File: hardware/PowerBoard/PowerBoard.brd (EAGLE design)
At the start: 90 x 56 mm, 134 parts, among them J1 CON-HRS-DM3AT, J2 CON-ZX62R-B-5P, J3 CON-FTSH-105-01-L-DV-K, J4 CON-S2B-PH-SM4-TB, J5 CON-PJ-102A, J6 CON-71741-0002-TOP, M1 MOUNT-HOLE3.3, M2 MOUNT-HOLE3.3, M3 MOUNT-HOLE3.3, M4 MOUNT-HOLE3.3, M5 FIDUCIAL1X2, M6 FIDUCIAL1X2, M7 FIDUCIAL1X2, M8 FIDUCIAL1X2, Q1 SI2323CDS, Q2 SI2312CDS, Q3 SI2333CDS, Q4 SI2333CDS, SW1 SWITCH-SPST, SW2 SWITCH-MS12ASG30, SW3 SWITCH-KSC-201J, U1 LTC4361-2DC, U10 MAX9938FEUK, U11 MAX9938FEUK, U12 MAX9938FEUK, U13 STM32F10XCXT6, U14 LTC2942-1, U15 USBLC6-2, U2 LTC4085, U3 XC6220B331MR-G, U4 XC6220B331MR-G, U5 XC9236A15DMR-G, U6 MIC94043, U8 MAX9938FEUK, U9 MAX9938FEUK, X1 ECX-2236, X2 ECX-31B

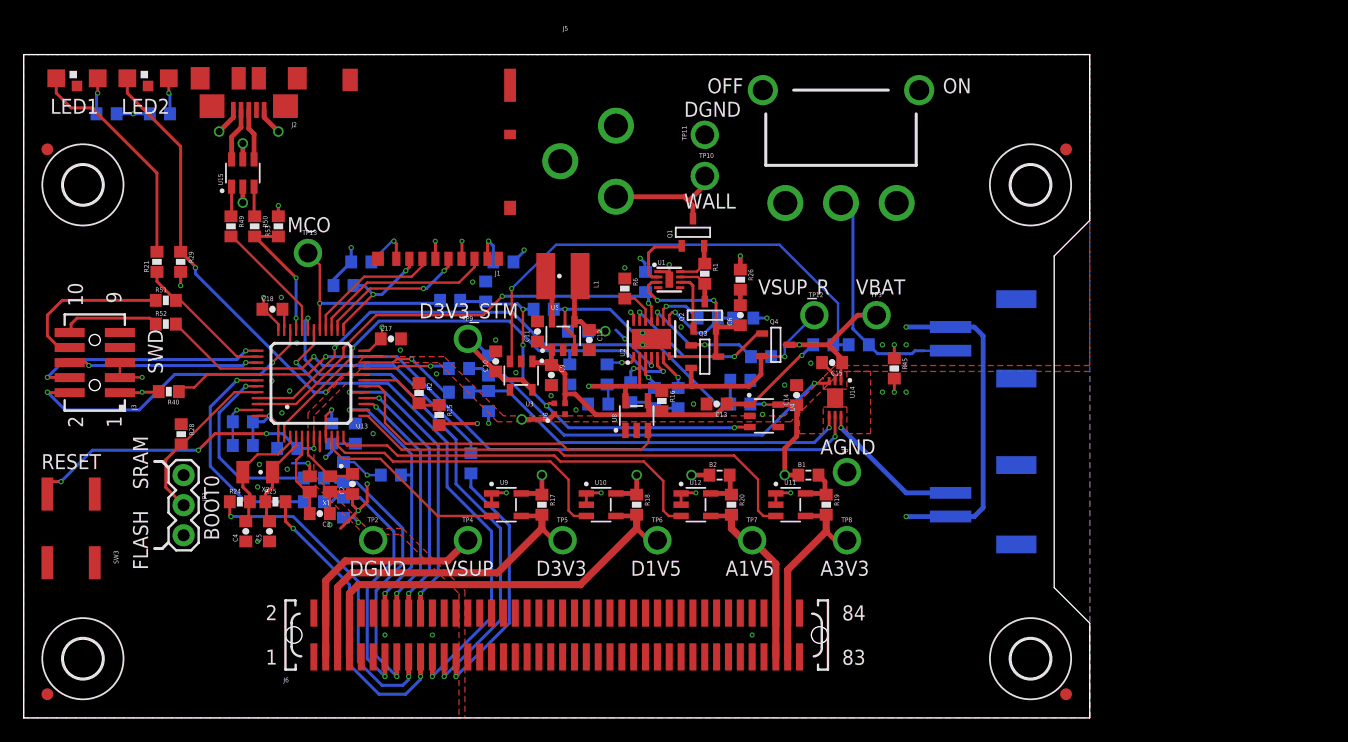
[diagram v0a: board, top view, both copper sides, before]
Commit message: - Interface updated on schematic
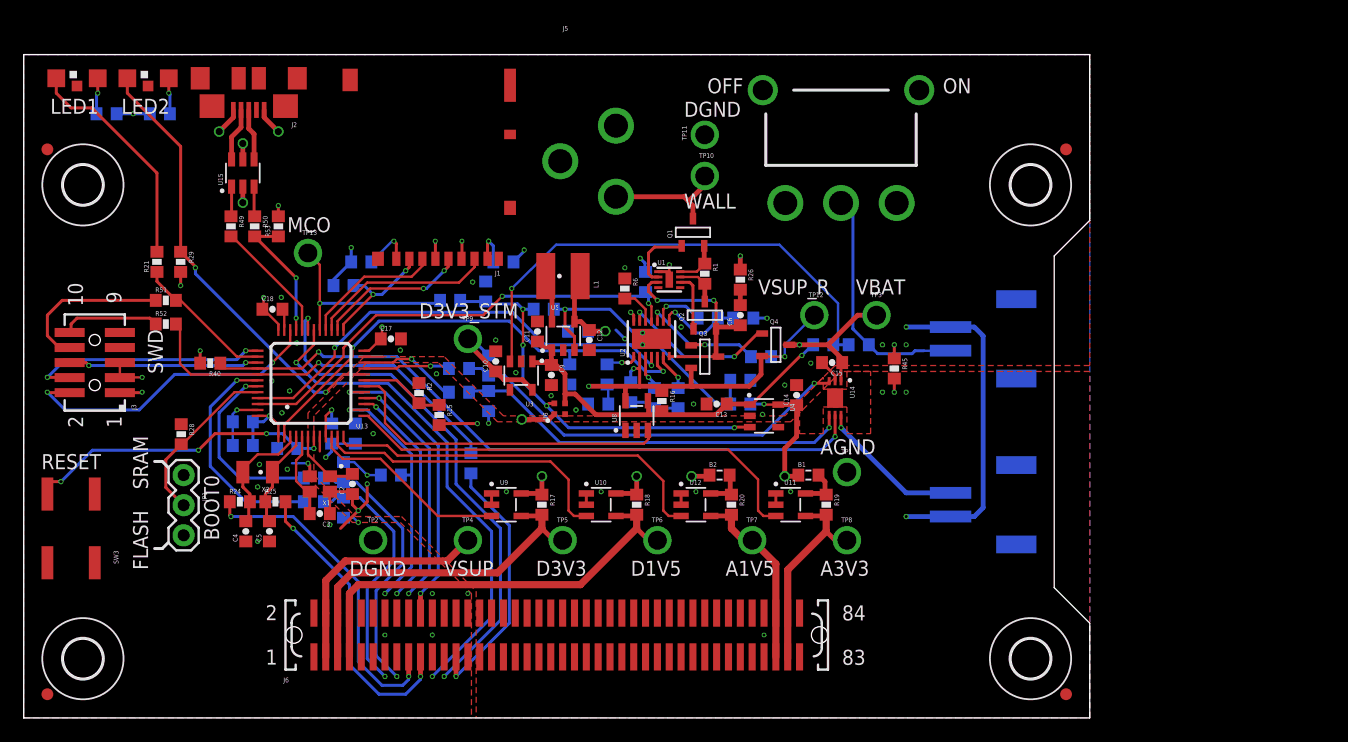
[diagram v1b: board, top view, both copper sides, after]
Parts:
- moved R40 4.24 mm to (15.8, 29.9)
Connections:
- net AGND: now also J6.77, J6.78; no longer J6.75, J6.76
- net DGND: now also J6.10, J6.15, J6.16, J6.9; no longer J6.11, J6.12, J6.22
- net I2C1_SCL: now also J6.26; no longer J6.13
- net I2C1_SDA: now also J6.28; no longer J6.15
- net PA10: now also J6.21; no longer J6.23
- net PA9: now also J6.23; no longer J6.21
- net PB4: now also R40.1, U14.5; no longer R48.2, R52.2
- net PB5: now also R48.2, R52.2; no longer R40.1, U14.5
- net SPI1_MISO: now also J6.22; no longer J6.18
- net SPI1_NSS: now also J6.24; no longer J6.14
- net SPI1_SCK: now also J6.18; no longer J6.16
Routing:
- net PB5: track 61.3 -> 32.0 mm, vias 2 -> 1
- net PB4: track 30.8 -> 58.3 mm, vias 1 -> 2
- net AGND: track 14.8 -> 9.76 mm
- net SPI1_SCK: track 20.9 -> 19.2 mm
- net SPI1_NSS: track 23.2 -> 21.6 mm
- net SPI1_MISO: track 21.9 -> 20.2 mm
- net PA9: track 43.9 -> 42.3 mm
- net PA10: track 45.3 -> 43.7 mm
- net I2C1_SDA: track 24.2 -> 22.6 mm
- net I2C1_SCL: track 22.7 -> 21.0 mm
- net VSUP_I_SENSE: track 29.0 -> 28.4 mm
- net D3V3_STM: track 50.8 -> 50.5 mm, vias 15 -> 16
- net DGND: vias 43 -> 45

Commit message: - Layout update - Interface update
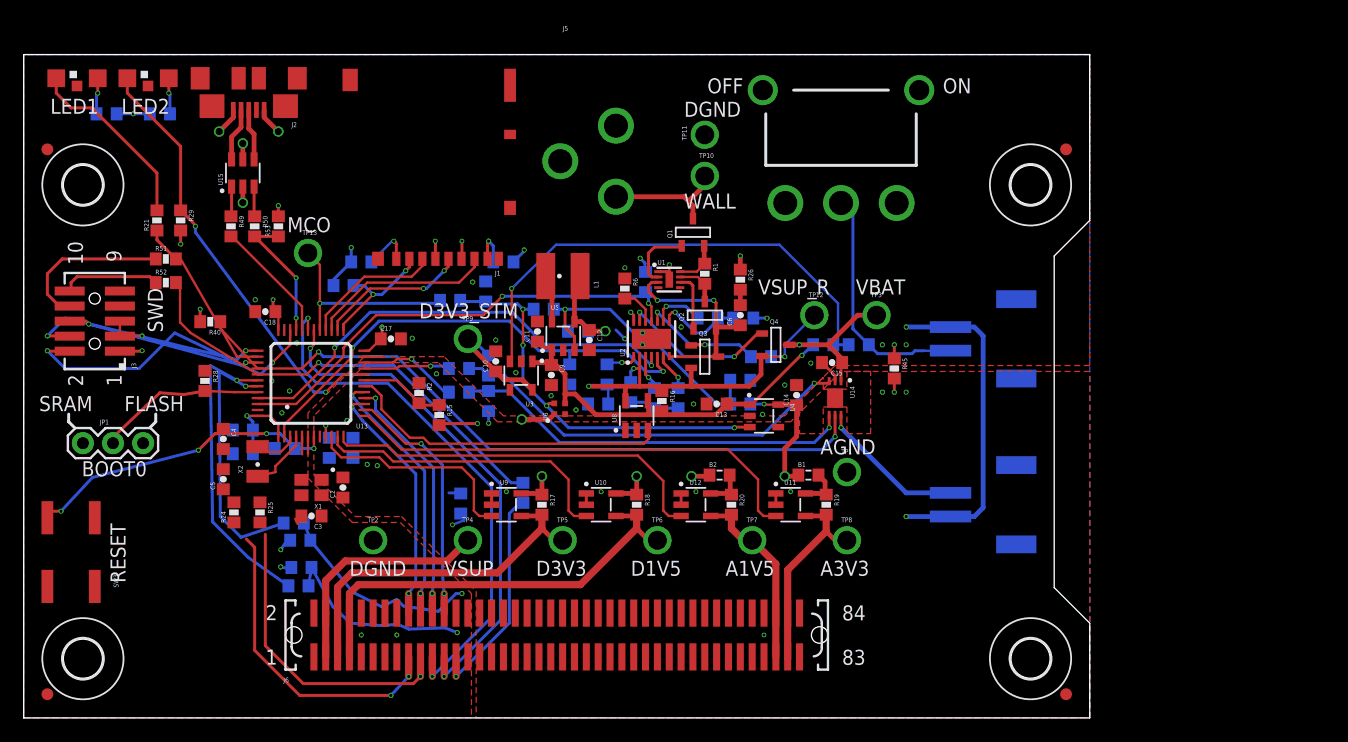
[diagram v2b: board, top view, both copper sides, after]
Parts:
- moved JP1 8.92 mm to (5.00, 23.2), turned to 0 degrees
- moved C4 8.03 mm to (16.9, 23.6), turned to 270 degrees
- moved R34 7.22 mm to (23.2, 11.2)
- moved R33 6.81 mm to (23.4, 15.0), turned to 0 degrees
- moved R30 6.37 mm to (36.9, 18.1), turned to 270 degrees
- moved R32 6.17 mm to (23.4, 12.7), turned to 0 degrees
- moved C5 5.88 mm to (16.9, 20.1)
- moved R48 5.06 mm to (42.1, 19.0)
- moved R28 4.92 mm to (15.3, 28.4)
- moved R35 4.16 mm to (22.8, 16.4)
- moved R40 3.50 mm to (15.8, 33.5)
- moved J3 3.50 mm to (6.00, 33.5)
- moved R21 3.50 mm to (11.2, 42.0)
- moved R29 3.50 mm to (13.2, 42.0)
- moved R51 3.50 mm to (12.0, 38.8)
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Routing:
- net DGND: track 71.1 -> 51.8 mm, vias 45 -> 35
- net D3V3_STM: track 50.5 -> 43.7 mm, vias 16 -> 17
- net I2C1_SCLI: track 19.1 -> 25.9 mm
- net PC14-S: track 10.2 -> 3.38 mm
- net I2C1_SDAI: track 15.8 -> 22.1 mm
- net PB5: track 32.0 -> 37.9 mm
- net OSC_IN: track 7.33 -> 1.50 mm
- net I2C1_SDA: track 22.6 -> 17.7 mm
- net AGND: track 9.76 -> 5.15 mm
- net OSC_OUT: track 6.10 -> 1.50 mm
- net I2C1_SCL: track 21.0 -> 17.3 mm
- net PB4-SF: track 22.0 -> 18.5 mm
- net PA15-LED1: track 19.5 -> 16.0 mm
- net SPI1_MOSI: track 25.4 -> 22.1 mm
- net PC15-S: track 8.52 -> 5.27 mm
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
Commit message: - Layout update
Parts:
- moved TP2 17.0 mm to (12.5, 15.0)
- moved TP4 17.0 mm to (20.5, 15.0)
- moved TP5 17.0 mm to (28.5, 15.0)
- moved TP6 17.0 mm to (36.5, 15.0)
- moved R17 10.0 mm to (33.8, 18.0)
- moved R18 10.0 mm to (41.8, 18.0)
- moved U10 10.0 mm to (38.8, 18.0)
- moved U9 10.0 mm to (30.8, 18.0)
- moved TP7 8.00 mm to (53.5, 15.0)
- moved TP8 8.00 mm to (61.5, 15.0)
- moved B2 7.50 mm to (51.2, 20.5)
- moved R19 7.50 mm to (60.2, 18.0)
- moved U11 7.50 mm to (57.2, 18.0)
- moved R20 7.30 mm to (52.5, 18.0)
- moved U12 7.30 mm to (49.5, 18.0)
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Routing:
- net D1V5: track 37.0 -> 24.4 mm
- net D3V3: track 30.3 -> 18.7 mm
- net D3V3_I: track 36.9 -> 47.8 mm
- net D1V5_SENSE: track 25.7 -> 15.7 mm
- net D3V3_SENSE: track 18.4 -> 8.76 mm
- net I2C1_SCLI: track 25.9 -> 16.4 mm
- net I2C1_SDA: track 17.7 -> 26.1 mm
- net PB4-SF: track 18.5 -> 10.6 mm
- net A3V3_SENSE: track 39.5 -> 32.0 mm
- net A1V5_SENSE: track 32.6 -> 25.3 mm
- net PB5: track 37.9 -> 44.9 mm
- net I2C1_SDAI: track 22.1 -> 15.2 mm
- net A1V5: track 15.8 -> 21.8 mm
- net VSUP: track 34.9 -> 39.7 mm
- net NRST: track 26.2 -> 30.2 mm, vias 4 -> 2
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
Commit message: - Layout
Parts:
- moved C4 3.61 mm to (16.8, 19.1)
- moved R28 2.55 mm to (13.2, 24.1)
- moved R32 1.71 mm to (26.1, 12.6), turned to 180 degrees
- moved R33 1.64 mm to (23.1, 12.6), turned to 0 degrees
- moved R40 1.53 mm to (17.2, 30.8), turned to 90 degrees
- moved C2 1.48 mm to (26.8, 18.4)
- moved R24 1.29 mm to (15.6, 15.1)
- moved R25 1.25 mm to (17.6, 15.1)
- moved C16 1.12 mm to (21.1, 22.2)
- moved R34 0.95 mm to (25.6, 15.1)
- moved R35 0.95 mm to (23.6, 15.1)
- moved C5 0.92 mm to (20.9, 18.4), turned to 90 degrees
- moved X1 0.92 mm to (24.2, 20.1)
- moved C3 0.76 mm to (24.2, 17.6)
- moved X2 0.36 mm to (19.8, 21.1), turned to 180 degrees
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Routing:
- net I2C1_SDA: track 26.1 -> 18.8 mm
- net OSC_IN: track 1.50 -> 6.10 mm
- net OSC_OUT: track 1.50 -> 5.37 mm
- net I2C1_SCL: track 19.2 -> 16.0 mm
- net D3V3_STM: track 42.5 -> 44.8 mm, vias 16 -> 17
- net TRACESWO: track 16.5 -> 18.4 mm
- net PC14-S: track 3.36 -> 4.61 mm
- net PC15-S: track 4.36 -> 3.16 mm
- net I2C1_SDAI: track 15.2 -> 14.1 mm
- net PC15: track 26.4 -> 25.4 mm
- net PC14: track 28.6 -> 27.6 mm
- net SWCLK: track 20.6 -> 21.5 mm
- net NRST: track 30.2 -> 30.9 mm
- net PB5: track 44.9 -> 44.3 mm
- net SWDIO: track 25.3 -> 25.8 mm

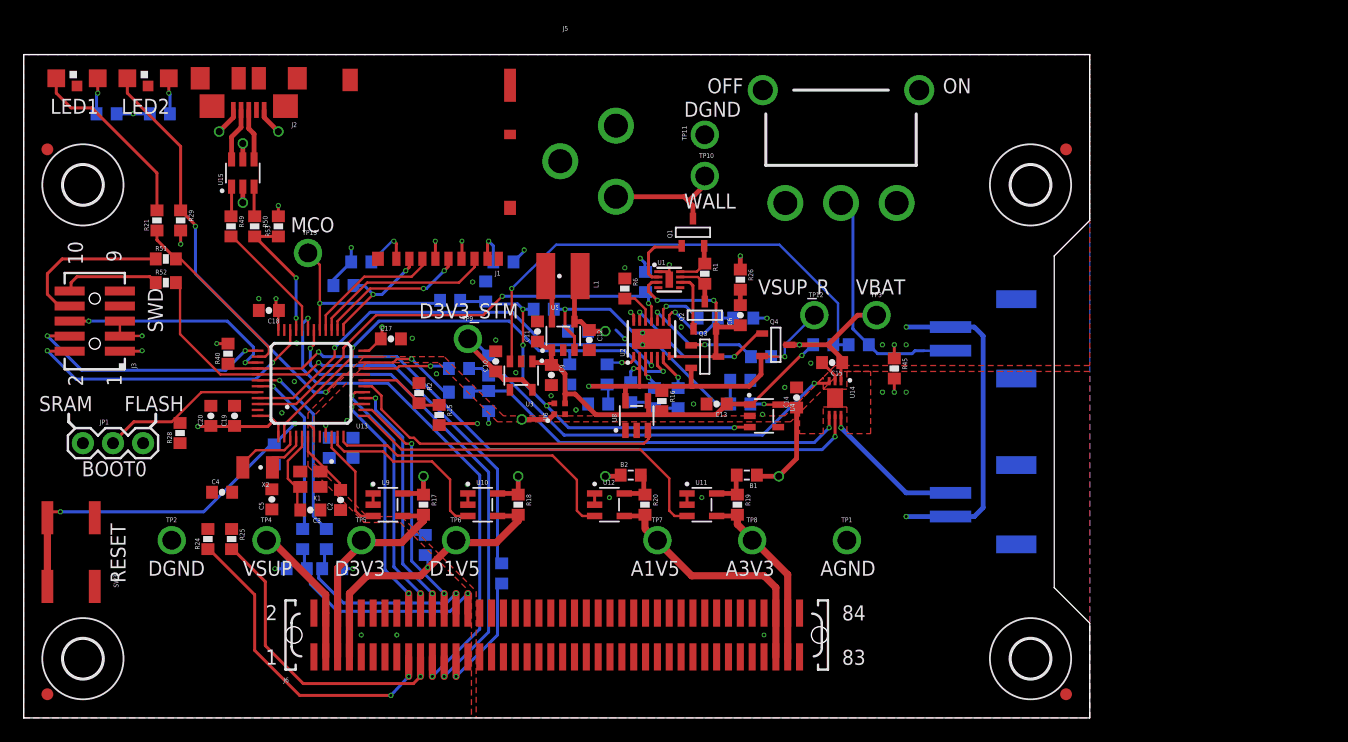
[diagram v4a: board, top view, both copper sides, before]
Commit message: - Components moved out of the bottom keep-out-box representing the battery - All grounds connected to mezzanine interface
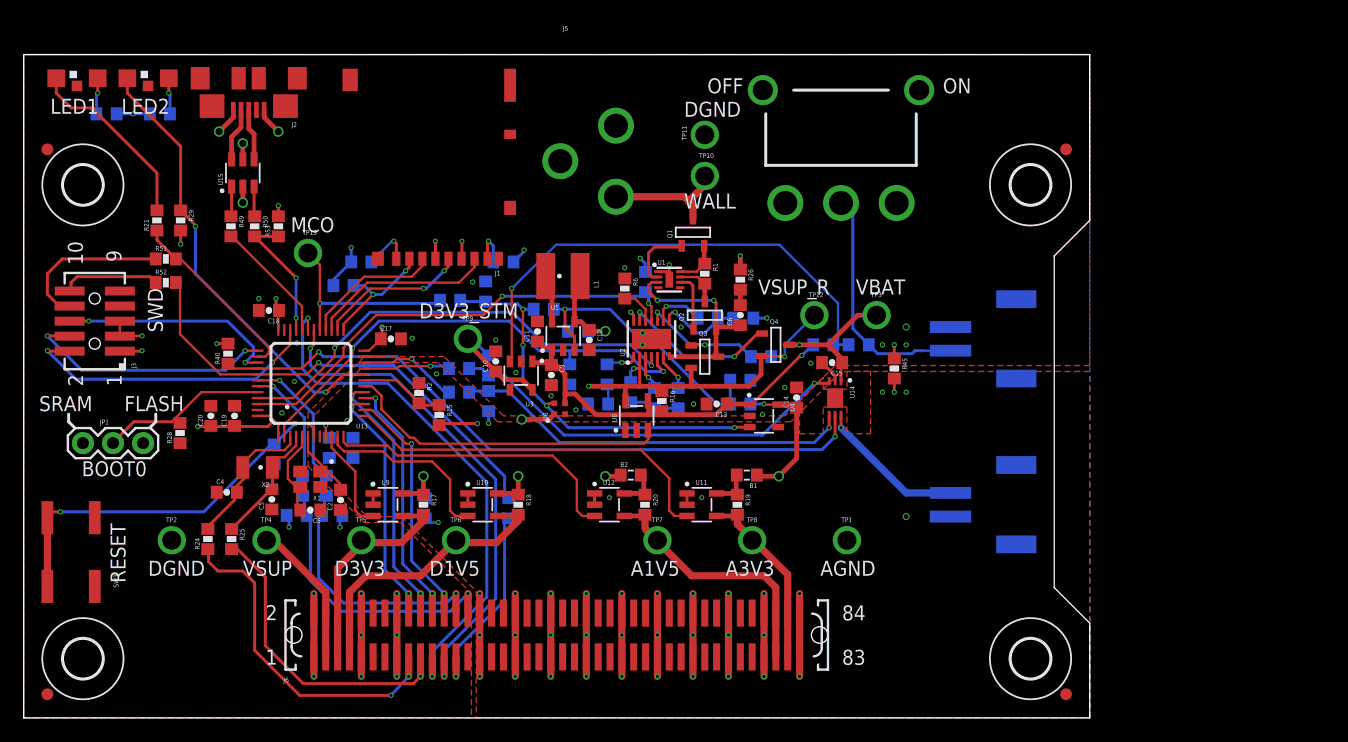
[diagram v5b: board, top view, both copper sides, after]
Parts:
- moved R48 5.53 mm to (41.0, 17.7)
- moved R32 4.50 mm to (26.1, 17.1)
- moved R33 4.50 mm to (23.1, 17.1)
- moved R34 4.50 mm to (25.6, 19.6)
- moved R35 4.50 mm to (23.6, 19.6)
- moved R30 3.10 mm to (33.9, 17.7)
- moved C4 0.40 mm to (17.1, 19.1)
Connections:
- net AGND: now also J6.29, J6.30, J6.35, J6.36, J6.41, J6.42, J6.47, J6.48, J6.53, J6.54, J6.59, J6.60, J6.65, J6.66, J6.71, J6.72
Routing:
- net AGND: track 5.15 -> 75.2 mm, vias 10 -> 38
- net DGND: track 51.2 -> 43.3 mm, vias 33 -> 38
- net PB4-SF: track 10.6 -> 16.9 mm
- net PC15-S: track 3.16 -> 9.23 mm
- net PB5: track 44.3 -> 38.6 mm
- net PC14-S: track 4.61 -> 9.92 mm
- net I2C1_SCL: track 16.0 -> 21.0 mm
- net I2C1_SDA: track 18.8 -> 23.3 mm
- net I2C1_SDAI: track 14.1 -> 9.60 mm
- net I2C1_SCLI: track 16.0 -> 11.5 mm

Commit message: - Minor changes in layout
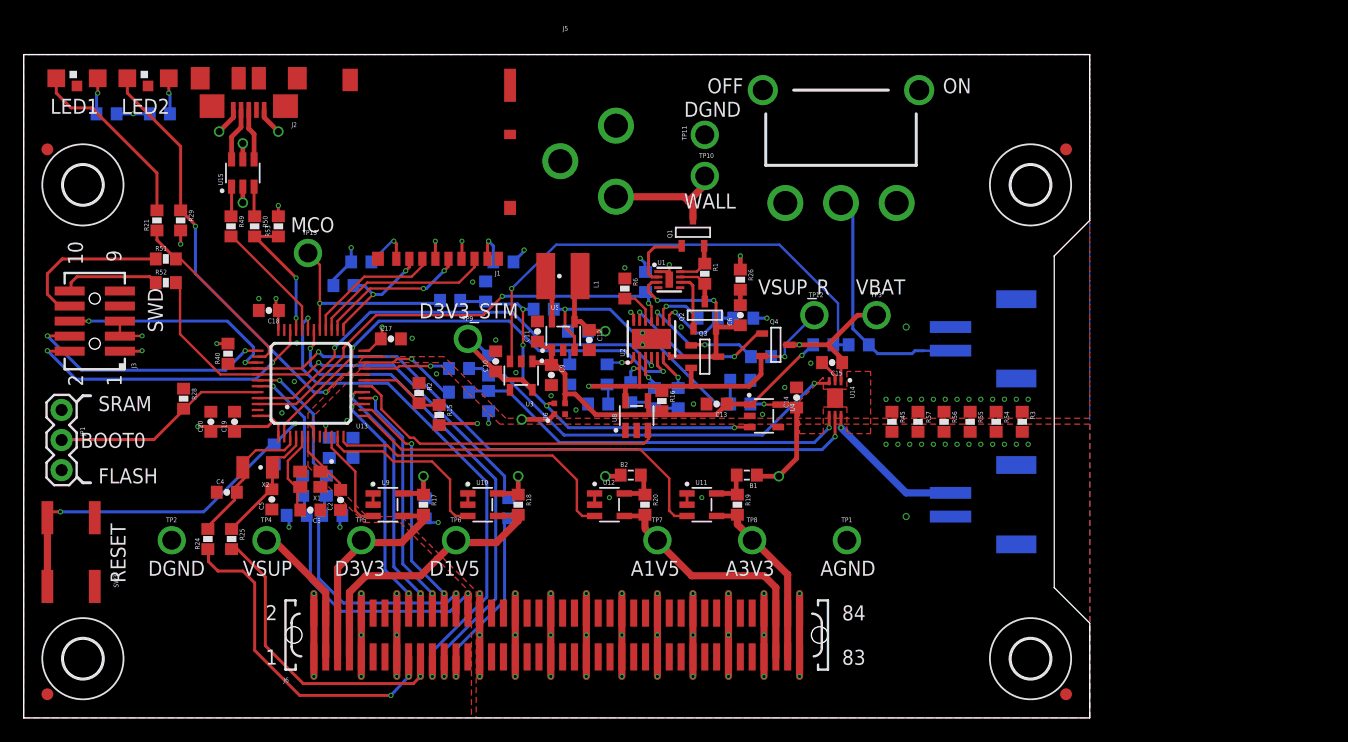
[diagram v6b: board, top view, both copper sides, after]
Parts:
- added R3, R54, R55, R56, R57: 0, powerboard:R0603
- moved R45 4.50 mm to (73.3, 25.0)
- moved JP1 3.33 mm to (3.20, 26.0), turned to 270 degrees
- moved R28 2.92 mm to (13.5, 26.9), turned to 270 degrees
- moved LOGO1 2.00 mm to (75.0, 12.2)
- moved LOGO7 1.50 mm to (75.0, 28.0)
- moved C19 0.50 mm to (17.8, 25.0)
- moved C20 0.50 mm to (15.8, 25.0)
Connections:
- net AGND: now also R3.2, R54.2, R55.2, R56.2, R57.2
- net DGND: now also R3.1, R54.1, R55.1, R56.1, R57.1
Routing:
- net BOOT0: track 13.6 -> 17.6 mm
- net AGND: track 75.2 -> 74.0 mm, vias 38 -> 48
- net DGND: track 43.3 -> 42.2 mm, vias 38 -> 48

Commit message: - Layout update
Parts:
- removed R21, R48: 0, powerboard:R0603
- removed R51, R52: DNP, powerboard:R0603
- added TP14: TESTPOINT, powerboard:TESTPOINT
- moved LOGO5 71.7 mm to (35.0, 63.5)
- moved LOGO6 63.6 mm to (23.0, 63.5)
- moved LOGO1 53.5 mm to (59.0, 63.2)
- moved LOGO7 44.8 mm to (47.0, 63.0)
- moved R40 32.8 mm to (48.9, 21.9), flipped to the bottom, turned to 180 degrees
- moved TP12 27.5 mm to (40.8, 25.0)
- moved R3 21.1 mm to (105.3, 23.0)
- moved R45 21.1 mm to (94.3, 23.0)
- moved R54 21.1 mm to (103.1, 23.0)
- moved R55 21.1 mm to (100.9, 23.0)
- moved R56 21.1 mm to (98.7, 23.0)
- moved R57 21.1 mm to (96.5, 23.0)
- moved TP1 13.0 mm to (74.5, 3.00)
- moved TP2 12.6 mm to (16.5, 3.00)
- moved U9 10.9 mm to (20.9, 13.4)
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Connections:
- removed net PA15-LED1: LED1.1, R21.2
- removed net PB4-SF: J6.25, R48.1
- net AGND: no longer R2.1, U10.1, U10.2, U8.1, U8.2, U9.1, U9.2
- net DGND: now also R2.1, U10.1, U10.2, U8.1, U8.2, U9.1, U9.2
- net JNTRST: no longer R52.1
- net JTDI: no longer R51.1
- net PA15: now also LED1.1; no longer R21.1, R51.2
- net PB5: now also J6.25; no longer R48.2, R52.2
- net VBUS: now also TP14.1
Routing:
- net D3V3_I: track 47.8 -> 86.6 mm
- net D1V5_I: track 29.0 -> 67.0 mm
- net VSUP: track 39.9 -> 62.5 mm
- net PA15: track 15.2 -> 37.0 mm
- net D3V3_SENSE: track 8.76 -> 25.8 mm
- net PB4-SF: track 16.9 -> 0.00 mm, vias 1 -> 0
- net PA15-LED1: track 16.0 -> 0.00 mm
- net JTDI: track 14.0 -> 1.15 mm
- net PB4: track 57.6 -> 45.7 mm, vias 2 -> 1
- net DGND: track 42.2 -> 53.6 mm
- net VSUP_R: track 45.9 -> 34.9 mm, vias 4 -> 3
- net D3V3: track 18.7 -> 10.00 mm
- net VSUP_I: track 30.6 -> 39.2 mm
- net JNTRST: track 8.31 -> 0.00 mm
- net D1V5: track 24.5 -> 16.4 mm
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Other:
- board text added: "VBUS"

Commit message: - Layout update
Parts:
- moved TP11 27.6 mm to (85.0, 52.0)
- moved TP12 25.1 mm to (65.7, 28.4)
- moved R40 19.8 mm to (68.7, 21.8)
- moved U9 14.5 mm to (34.6, 18.2), turned to 180 degrees
- moved R30 11.6 mm to (24.3, 17.6)
- moved R17 8.90 mm to (31.5, 18.2), turned to 90 degrees
- moved R32 8.01 mm to (22.3, 17.6)
- moved R33 8.01 mm to (19.4, 17.6)
- moved R34 8.01 mm to (21.9, 20.6)
- moved R35 8.01 mm to (19.9, 20.6)
- moved C18 7.75 mm to (18.5, 34.0)
- moved B2 7.62 mm to (59.1, 15.4)
- moved R20 7.62 mm to (59.9, 12.9)
- moved U12 7.62 mm to (56.8, 12.9)
- moved TP7 7.42 mm to (62.2, 13.2)
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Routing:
- net SPI1_NSS: track 20.2 -> 34.5 mm
- net D3V3_SENSE: track 25.8 -> 12.8 mm
- net A1V5_SENSE: track 22.9 -> 34.0 mm
- net SPI1_MISO: track 19.7 -> 30.3 mm
- net D3V3_I: track 86.6 -> 76.2 mm
- net I2C1_SDA: track 20.4 -> 30.2 mm
- net PB5: track 35.0 -> 44.8 mm
- net PA10: track 42.0 -> 51.7 mm
- net PA9: track 41.3 -> 50.8 mm
- net I2C1_SCL: track 18.0 -> 27.4 mm
- net A1V5: track 18.5 -> 11.1 mm
- net PC13: track 40.6 -> 47.7 mm
- net SPI1_MOSI: track 20.7 -> 27.8 mm
- net D1V5_I: track 67.0 -> 74.0 mm
- net PB9: track 35.5 -> 42.5 mm
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- added copper zone on layer 1, net N$6
